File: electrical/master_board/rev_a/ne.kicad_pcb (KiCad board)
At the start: 2 copper layers, 42.7 x 39.4 mm, 8 parts, among them CN105 BRIDGE_NE_OUTER;2xM1x1+M1x5, CN60 HCSR04;F1x4H

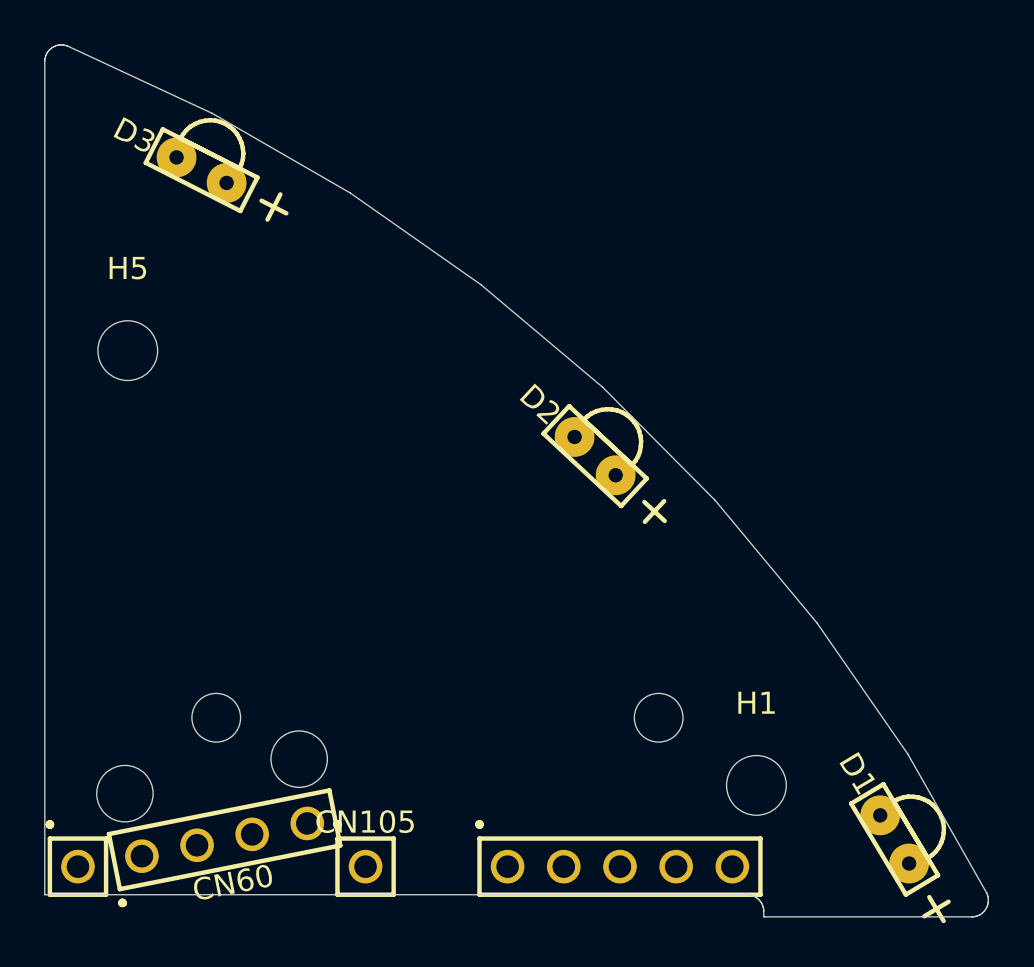
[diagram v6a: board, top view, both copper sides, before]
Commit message: The four corner boards ne/nw/se/sw are now zoned.
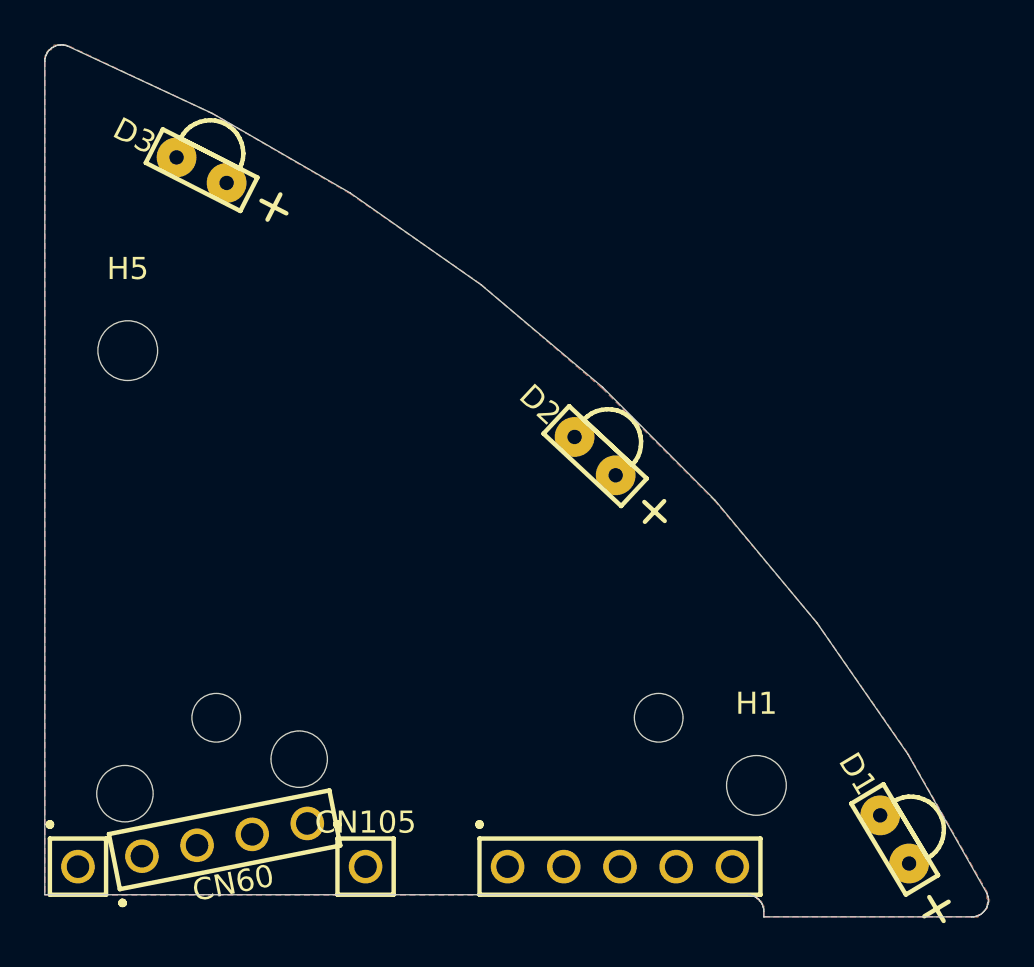
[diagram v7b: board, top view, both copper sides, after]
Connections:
- net Net-(CN105-Pad1) renamed /GND
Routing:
- added copper zone on B.Cu, net /GND
- added copper zone on F.Cu, net /GND
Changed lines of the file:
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@@
   (net 9 "Net-(CN105-Pad3)")
   (net 10 "Net-(CN105-Pad2)")
-  (net 11 "Net-(CN105-Pad1)")
+  (net 11 /GND)
   (net_class Default "This is the default net class."
     (clearance 0.2)
@@
     (uvia_dia 0.3)
     (uvia_drill 0.1)
-    (add_net "Net-(CN105-Pad1)")
+    (add_net /GND)
     (add_net "Net-(CN105-Pad2)")
     (add_net "Net-(CN105-Pad3)")
@@
       (net 10 "Net-(CN105-Pad2)"))
     (pad 1 thru_hole circle (at -13 0) (size 1.52 1.52) (drill 1.02) (layers *.Cu *.Mask)
-      (net 11 "Net-(CN105-Pad1)"))
+      (net 11 /GND))
   )
   (module HR2:LED_GRNRA (layer F.Cu)
@@
   (gr_line (start 162.5 63.68) (end 162.5 63.75) (layer Edge.Cuts) (width 0.05))
   (gr_line (start 162.5 63.75) (end 162.5 64) (layer Edge.Cuts) (width 0.05))
+  (zone (net 11) (net_name /GND) (layer F.Cu) (hatch edge 0.508)
+    (connect_pads (clearance 0.508))
+    (min_thickness 0.254)
+    (fill yes (arc_segments 32) (thermal_gap 0.508) (thermal_bridge_width 0.508))
+    (polygon
+      (pts
+        (xy 162.5 64) (xy 171.9 64) (xy 172 64) (xy 172 64)
+        (xy 172.1 64) (xy 172.2 64) (xy 172.2 63.9) (xy 172.3 63.9)
+        (xy 172.3 63.9) (xy 172.4 63.8) (xy 172.4 63.8) (xy 172.5 63.7)
+        (xy 172.5 63.7) (xy 172.6 63.6) (xy 172.6 63.6) (xy 172.6 63.5)
+        (xy 172.6 63.4) (xy 172.6 63.4) (xy 172.7 63.3) (xy 172.7 63.2)
+        (xy 172.6 63.2) (xy 172.6 63.1) (xy 172.6 63) (xy 172.6 63)
+        (xy 172.6 62.9) (xy 172.6 62.9) (xy 169 56.6) (xy 164.9 50.7)
+        (xy 160.3 45.2) (xy 155.2 40.1) (xy 149.7 35.4) (xy 143.8 31.3)
+        (xy 137.6 27.7) (xy 131 24.6) (xy 131 24.6) (xy 130.9 24.6)
+        (xy 130.8 24.6) (xy 130.8 24.6) (xy 130.7 24.6) (xy 130.6 24.6)
+        (xy 130.6 24.6) (xy 130.5 24.6) (xy 130.4 24.6) (xy 130.4 24.7)
+        (xy 130.3 24.7) (xy 130.3 24.8) (xy 130.2 24.8) (xy 130.2 24.8)
+        (xy 130.1 24.9) (xy 130.1 25) (xy 130.1 25) (xy 130 25.1)
+        (xy 130 25.1) (xy 130 25.2) (xy 130 25.3) (xy 130 25.3)
+        (xy 130 63) (xy 161.8 63) (xy 161.8 63) (xy 161.9 63)
+        (xy 161.9 63) (xy 162 63) (xy 162.1 63.1) (xy 162.1 63.1)
+        (xy 162.2 63.1) (xy 162.2 63.2) (xy 162.3 63.2) (xy 162.3 63.3)
+        (xy 162.4 63.3) (xy 162.4 63.4) (xy 162.4 63.4) (xy 162.5 63.5)
+        (xy 162.5 63.6) (xy 162.5 63.6) (xy 162.5 63.7) (xy 162.5 63.8)
+      )
+    )
+  )
+  (zone (net 11) (net_name /GND) (layer B.Cu) (hatch edge 0.508)
+    (connect_pads (clearance 0.508))
+    (min_thickness 0.254)
+    (fill yes (arc_segments 32) (thermal_gap 0.508) (thermal_bridge_width 0.508))
+    (polygon
+      (pts
+        (xy 162.5 64) (xy 171.9 64) (xy 172 64) (xy 172 64)
+        (xy 172.1 64) (xy 172.2 64) (xy 172.2 63.9) (xy 172.3 63.9)
+        (xy 172.3 63.9) (xy 172.4 63.8) (xy 172.4 63.8) (xy 172.5 63.7)
+        (xy 172.5 63.7) (xy 172.6 63.6) (xy 172.6 63.6) (xy 172.6 63.5)
+        (xy 172.6 63.4) (xy 172.6 63.4) (xy 172.7 63.3) (xy 172.7 63.2)
+        (xy 172.6 63.2) (xy 172.6 63.1) (xy 172.6 63) (xy 172.6 63)
+        (xy 172.6 62.9) (xy 172.6 62.9) (xy 169 56.6) (xy 164.9 50.7)
+        (xy 160.3 45.2) (xy 155.2 40.1) (xy 149.7 35.4) (xy 143.8 31.3)
+        (xy 137.6 27.7) (xy 131 24.6) (xy 131 24.6) (xy 130.9 24.6)
+        (xy 130.8 24.6) (xy 130.8 24.6) (xy 130.7 24.6) (xy 130.6 24.6)
+        (xy 130.6 24.6) (xy 130.5 24.6) (xy 130.4 24.6) (xy 130.4 24.7)
+        (xy 130.3 24.7) (xy 130.3 24.8) (xy 130.2 24.8) (xy 130.2 24.8)
+        (xy 130.1 24.9) (xy 130.1 25) (xy 130.1 25) (xy 130 25.1)
+        (xy 130 25.1) (xy 130 25.2) (xy 130 25.3) (xy 130 25.3)
+        (xy 130 63) (xy 161.8 63) (xy 161.8 63) (xy 161.9 63)
+        (xy 161.9 63) (xy 162 63) (xy 162.1 63.1) (xy 162.1 63.1)
+        (xy 162.2 63.1) (xy 162.2 63.2) (xy 162.3 63.2) (xy 162.3 63.3)
+        (xy 162.4 63.3) (xy 162.4 63.4) (xy 162.4 63.4) (xy 162.5 63.5)
+        (xy 162.5 63.6) (xy 162.5 63.6) (xy 162.5 63.7) (xy 162.5 63.8)
+      )
+    )
+  )
 )
